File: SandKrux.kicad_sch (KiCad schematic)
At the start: 55 parts, among them CN1 527450697, J1 FH12-40S-0.5SH_55_, J2 Connector, USB-TYPE-C-16P, U1 K210_C913414, U2 AXP173, U3 MT9700-N, U5 GD25LQ128EWIGR, U6 TMI7003C, U7 SGM803-TXN3/TR_C5152602, X1 X322526MMB4SI

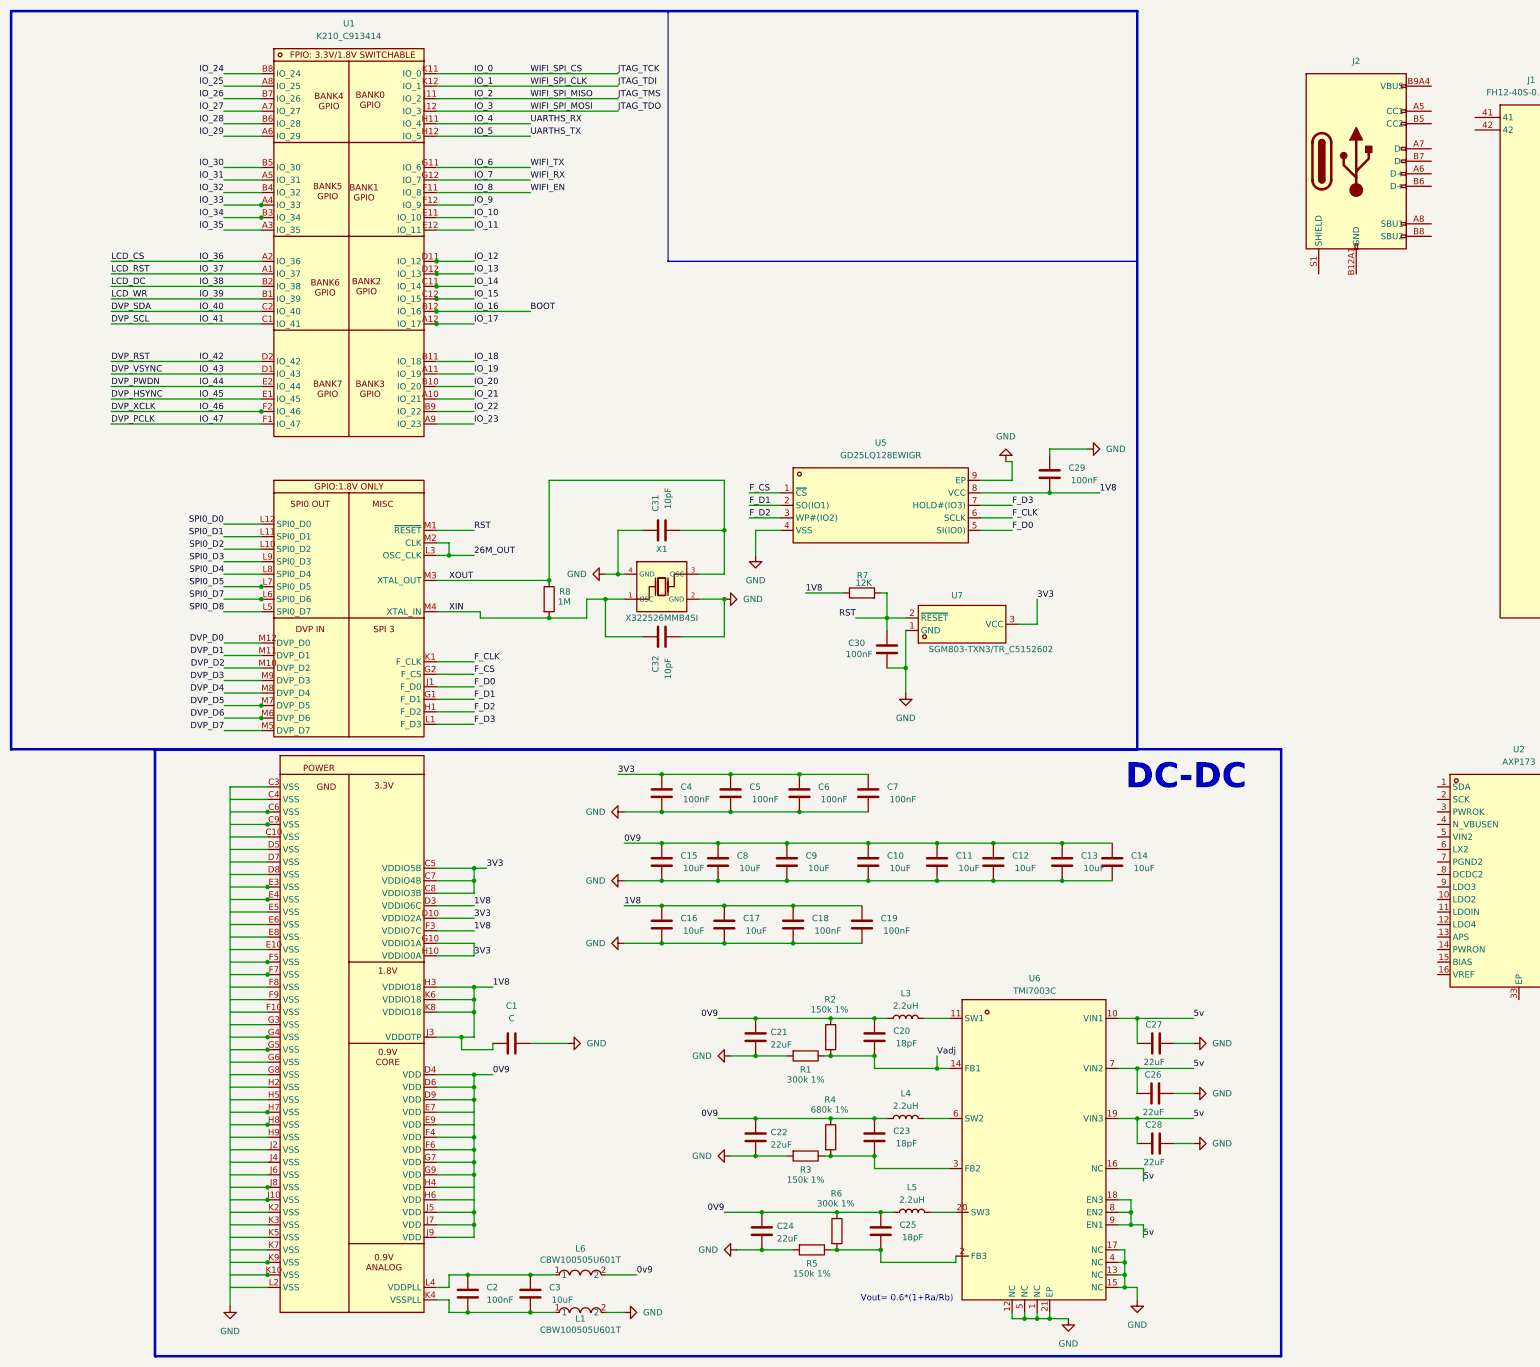
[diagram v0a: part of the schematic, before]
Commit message: camera suport
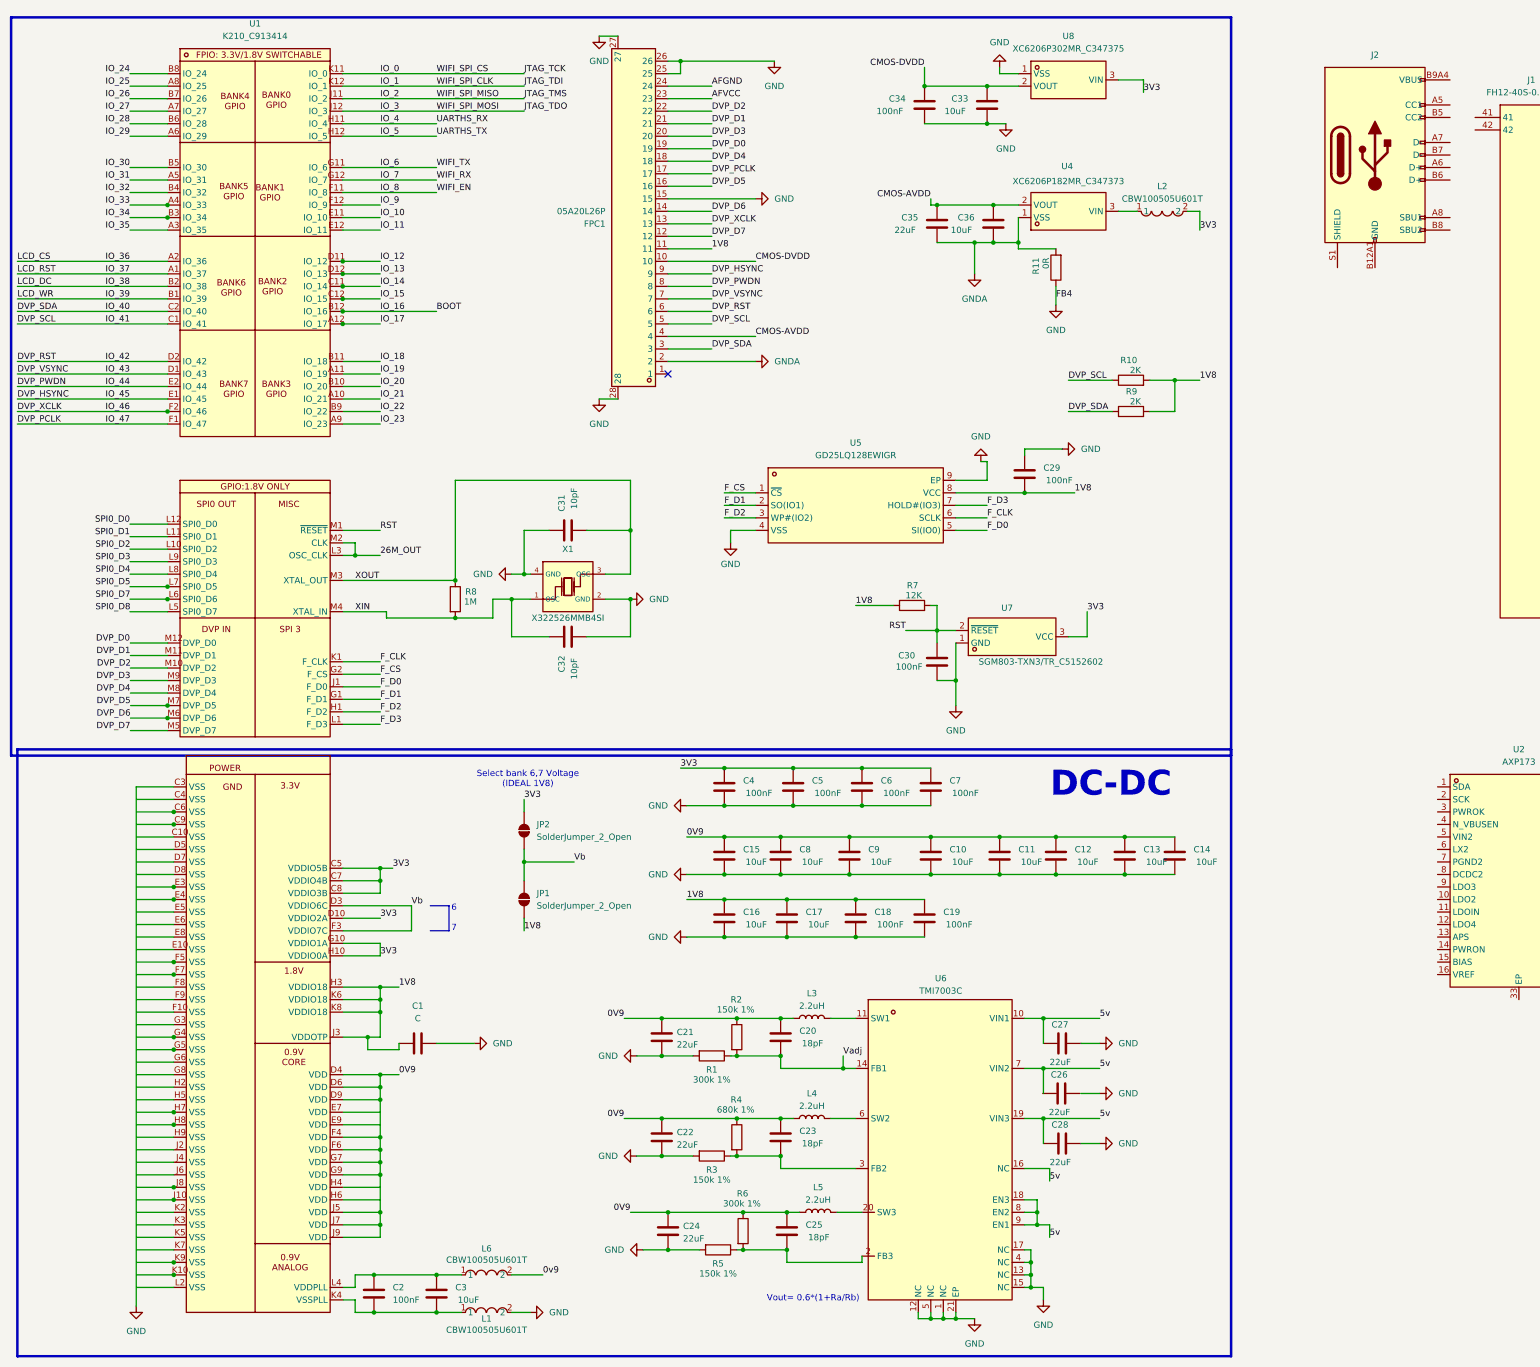
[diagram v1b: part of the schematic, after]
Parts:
- added C33, C36: 10uF, symbol Device:C
- added C34: 100nF, symbol Device:C
- added C35: 22uF, symbol Device:C
- added FPC1: 05A20L26P, easyeda2kicad:FPC-SMD_05A20L26P, symbol easyeda2kicad:05A20L26P
- added JP1, JP2: SolderJumper_2_Open, Jumper:SolderJumper-2_P1.3mm_Open_RoundedPad1.0x1.5mm, symbol Jumper:SolderJumper_2_Open
- added L2: CBW100505U601T, easyeda2kicad:L0402, symbol easyeda2kicad:CBW100505U601T
- added R10, R9: 2K, symbol Device:R
- added R11: 0R, symbol Device:R
- added U4: XC6206P182MR_C347373, easyeda2kicad:SOT-23-3_L3.0-W1.7-P0.95-LS2.9-BR, symbol easyeda2kicad:XC6206P182MR_C347373
- added U8: XC6206P302MR_C347375, easyeda2kicad:SOT-23-3_L3.0-W1.7-P0.95-LS2.9-BR, symbol easyeda2kicad:XC6206P302MR_C347375
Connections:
- net 1V8: now also FPC1.11, JP1.2 (B), R10.2, R9.2
- net DVP_D0: now also FPC1.19
- net DVP_D1: now also FPC1.21
- net DVP_D2: now also FPC1.22
- net DVP_D3: now also FPC1.20
- net DVP_D4: now also FPC1.18
- net DVP_D5: now also FPC1.16
- net DVP_D6: now also FPC1.14
- net DVP_D7: now also FPC1.12
- net DVP_HSYNC: now also FPC1.9
- net DVP_PCLK: now also FPC1.17
- net DVP_PWDN: now also FPC1.8
- net DVP_RST: now also FPC1.6
- net DVP_SCL: now also FPC1.5, R10.1
- net DVP_SDA: now also FPC1.3, R9.1
- net DVP_VSYNC: now also FPC1.7
- net DVP_XCLK: now also FPC1.13
- net GND: now also C33.1, C34.1, FPC1.15, FPC1.25, FPC1.26, FPC1.27, FPC1.28, R11.1, U8.1 (VSS)
- net at C4.2, C5.2, C6.2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: now also JP2.1 (A), L2.2, U8.3 (VIN)
- new net: L2.1, U4.3 (VIN)
- new net AFGND: FPC1.24
- new net AFVCC: FPC1.23
- new net CMOS-AVDD: C35.2, C36.2, FPC1.4, U4.2 (VOUT)
- new net CMOS-DVDD: C33.2, C34.2, FPC1.10, U8.2 (VOUT)
- new net GNDA: C35.1, C36.1, FPC1.2, R11.2, U4.1 (VSS)
- new net Vb: JP1.1 (A), JP2.2 (B)
- no-connect marks 0 -> 1
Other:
- note added: "6 7"
- note added: "Select bank 6,7 Voltage (IDEAL 1V8)"
- moved on the sheet: C1, C10, C11, C12, C13, C14, C15, C16, C17, C18, C19, C2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

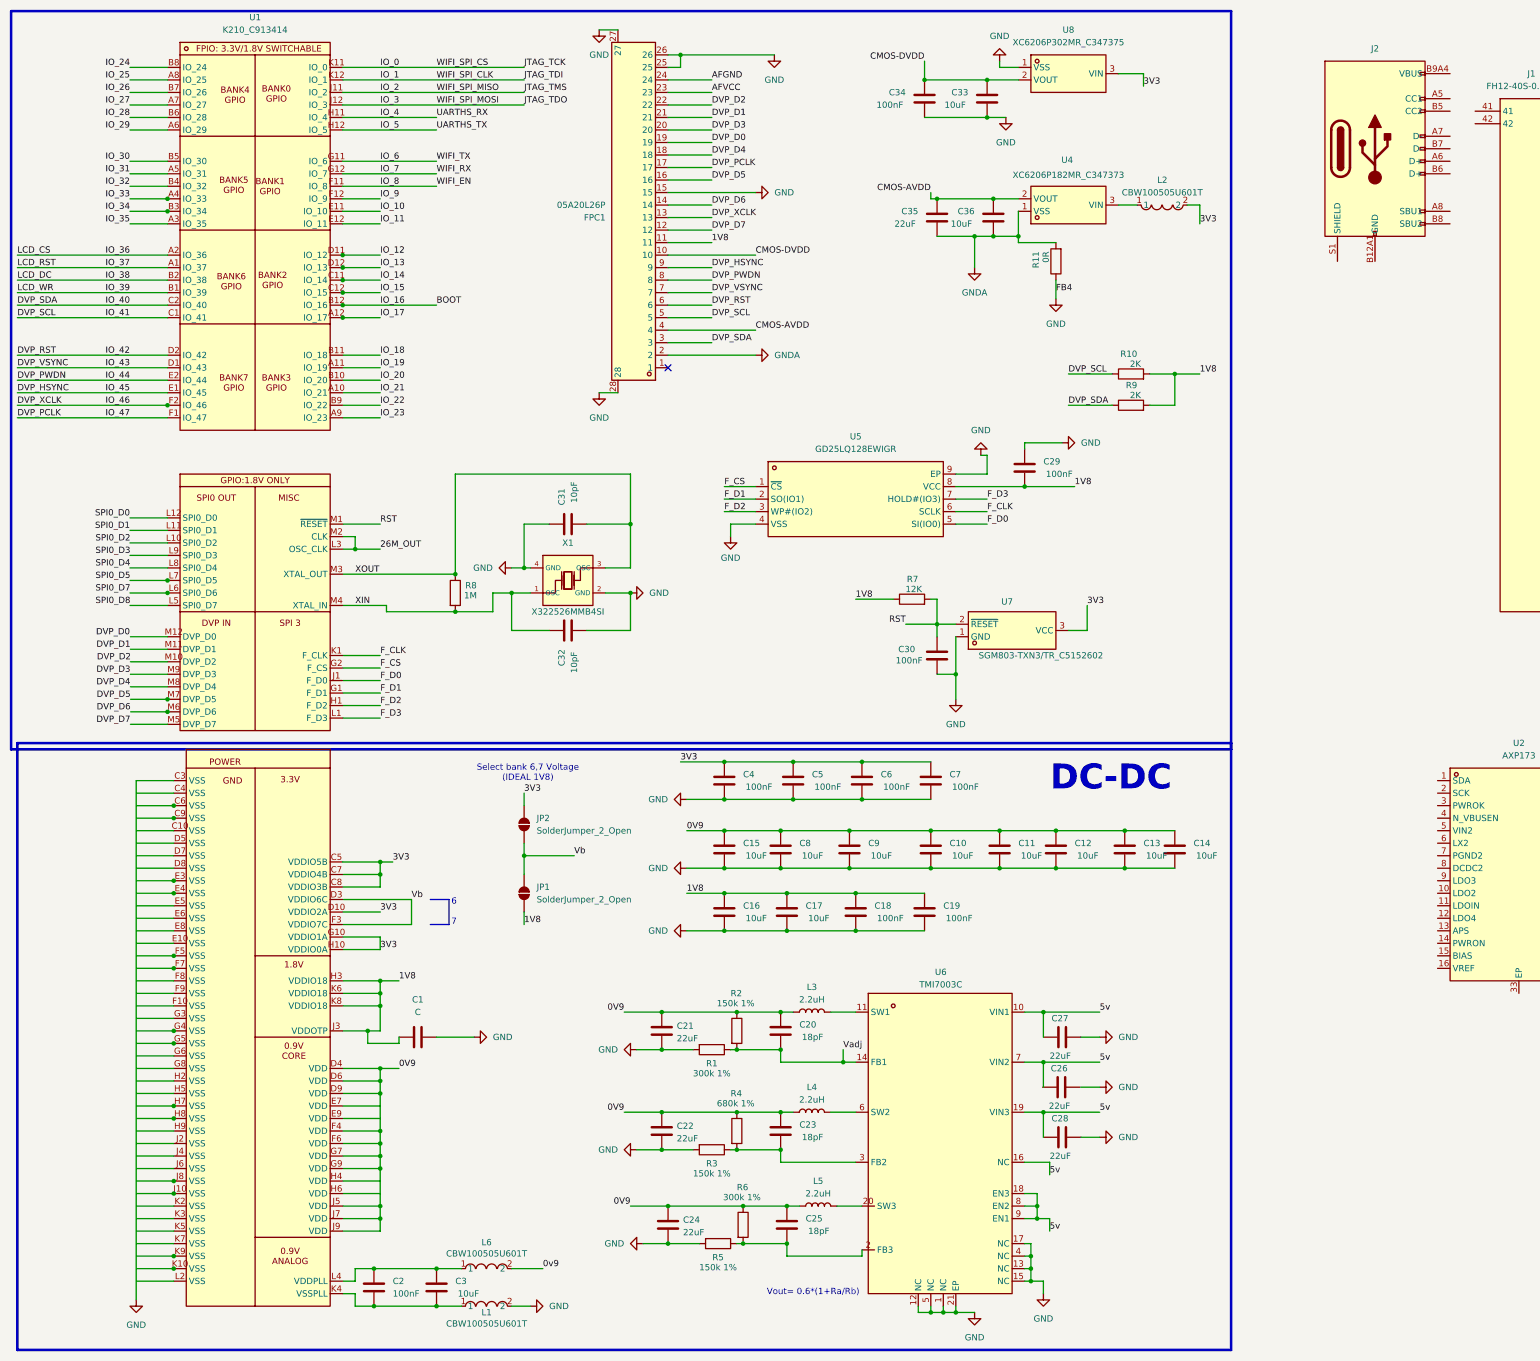
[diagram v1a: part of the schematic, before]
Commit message: organizacao basica dos componentes na pcb
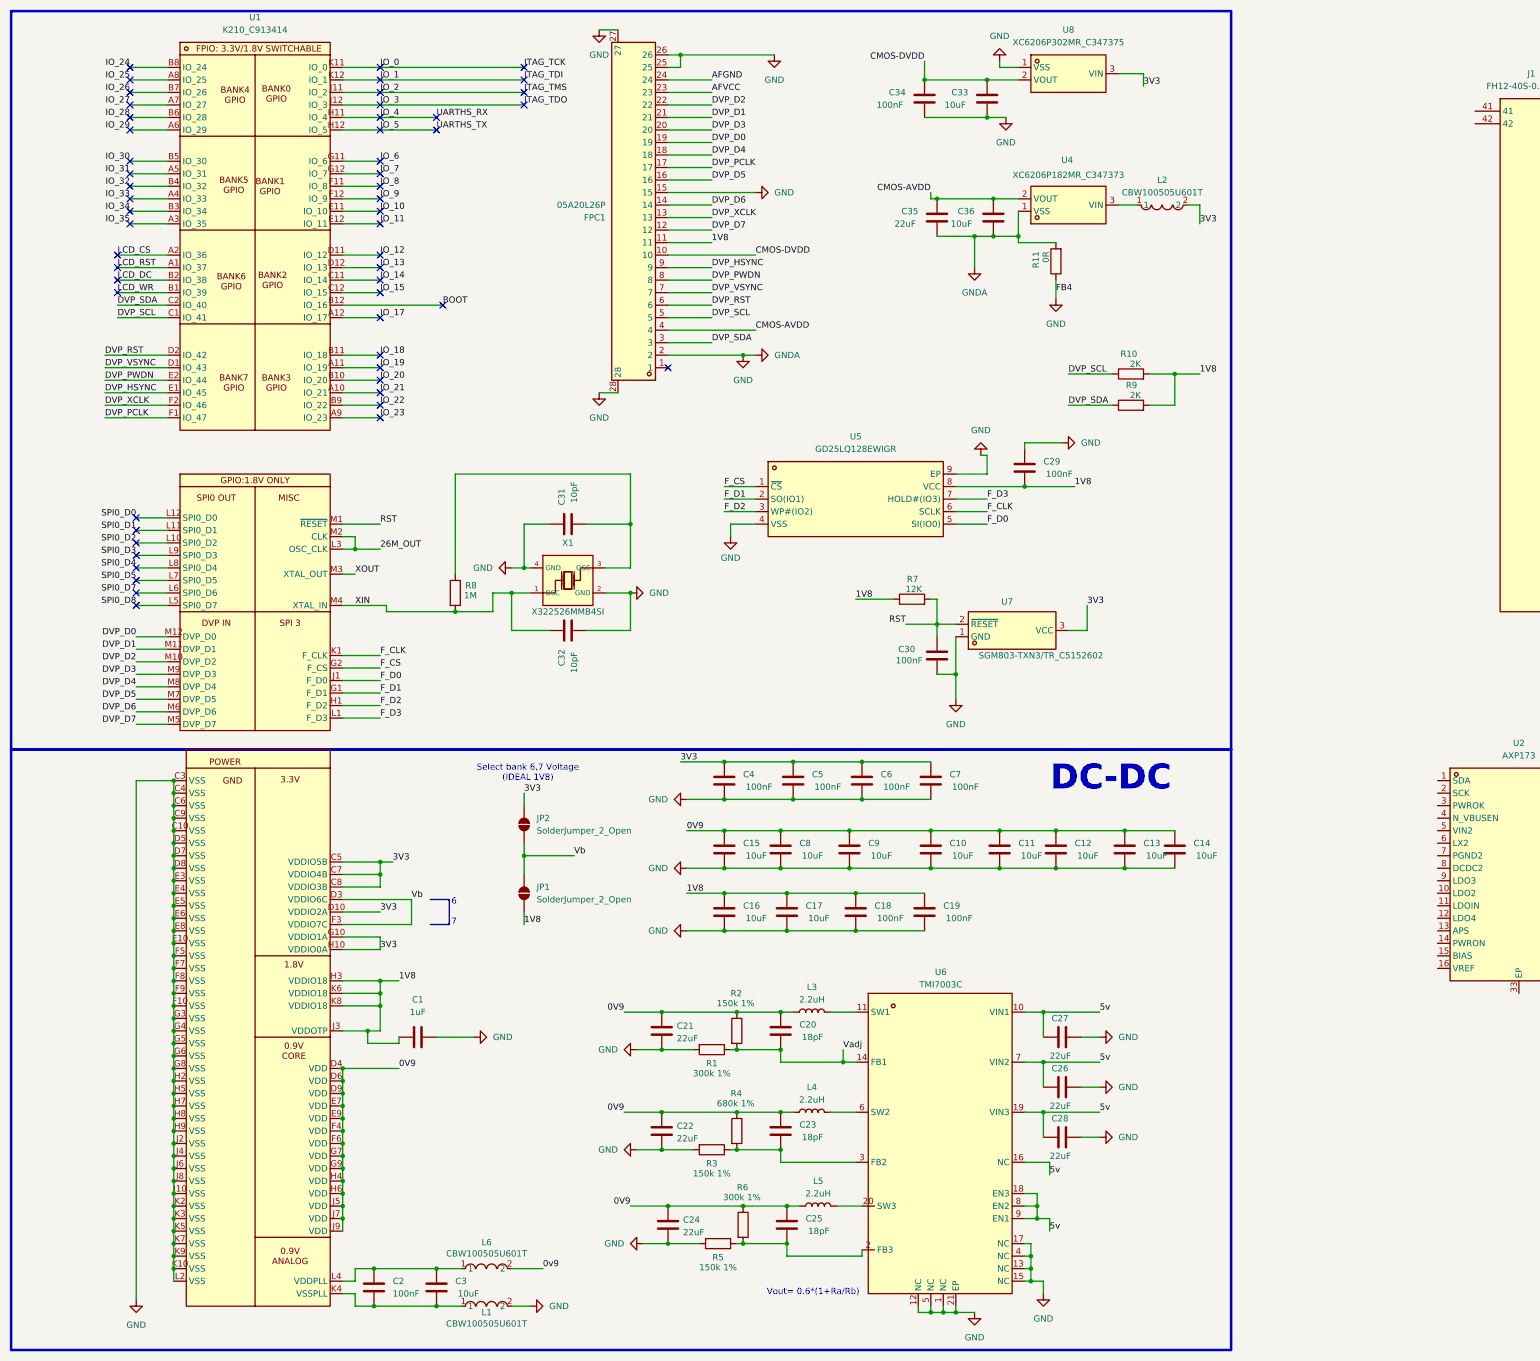
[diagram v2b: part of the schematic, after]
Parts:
- removed J2: Connector, USB-TYPE-C-16P, PCM_JLCPCB:TYPE-C-SMD_HX-TYPE-C-16PIN, symbol PCM_JLCPCB-Extended:Connector, USB-TYPE-C-16P
- C1: value C -> 1uF; footprint (none) -> Capacitor_SMD:C_0201_0603Metric
- C10, C11, C12, C13, C14, C15, C16, C17, C18, C19, C2, C20, C21, C22, C23, C24, C25, C26, C27, C28, C29, C3, C30, C31, C32, C33, C34, C35, C36, C4, C5, C6, C7, C8, C9: footprint (none) -> Capacitor_SMD:C_0201_0603Metric
- J1: footprint FH1240S05SH55 -> KiCad:FH1240S05SH55
- L3, L4, L5: footprint (none) -> Inductor_SMD:L_0805_2012Metric
- R1, R10, R11, R2, R3, R4, R5, R6, R7, R8, R9: footprint (none) -> Resistor_SMD:R_0201_0603Metric
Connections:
- net GNDA is gone; now on net GND: C35.1, C36.1, FPC1.2, R11.2, U4.1 (VSS)
- net 0V9: now also U1.D4 (VDD), U1.D6 (VDD), U1.D9 (VDD), U1.E7 (VDD), U1.E9 (VDD), U1.F4 (VDD), U1.F6 (VDD), U1.G7 (VDD), U1.G9 (VDD), U1.H4 (VDD), U1.H6 (VDD), U1.J5 (VDD), U1.J7 (VDD), U1.J9 (VDD)
- net 1V8: now also U1.H3 (VDDIO18), U1.J3 (VDDOTP), U1.K6 (VDDIO18), U1.K8 (VDDIO18)
- net 26M_OUT: now also U1.L3 (OSC_CLK), U1.M2 (CLK)
- net 5v: now also C26.2
- net DVP_D0: now also U1.M12 (DVP_D0)
- net F_CLK: now also U1.K1 (F_CLK)
- net F_CS: now also U1.G2 (F_CS)
- net F_D0: now also U1.J1 (F_D0)
- net F_D1: now also U1.G1 (F_D1)
- net F_D2: now also U1.H1 (F_D2)
- net F_D3: now also U1.L1 (F_D3)
- net GND: now also C26.1, U1.C10 (VSS), U1.C4 (VSS), U1.C6 (VSS), U1.C9 (VSS), U1.D5 (VSS), U1.D7 (VSS), U1.D8 (VSS), U1.E10 (VSS), U1.E3 (VSS), U1.E4 (VSS), U1.E5 (VSS), U1.E6 (VSS), U1.E8 (VSS), U1.F10 (VSS), U1.F5 (VSS), U1.F7 (VSS), U1.F8 (VSS), U1.F9 (VSS), U1.G3 (VSS), U1.G4 (VSS), U1.G5 (VSS), U1.G6 (VSS), U1.G8 (VSS), U1.H2 (VSS), U1.H5 (VSS), U1.H7 (VSS), U1.H8 (VSS), U1.H9 (VSS), U1.J10 (VSS), U1.J2 (VSS), U1.J4 (VSS), U1.J6 (VSS), U1.J8 (VSS), U1.K10 (VSS), U1.K2 (VSS), U1.K3 (VSS), U1.K5 (VSS), U1.K7 (VSS), U1.K9 (VSS), U1.L2 (VSS)
- net IO_18: now also U1.B11 (IO_18)
- net IO_19: now also U1.A11 (IO_19)
- net IO_20: now also U1.B10 (IO_20)
- net IO_21: now also U1.A10 (IO_21)
- net IO_22: now also U1.B9 (IO_22)
- net IO_23: now also U1.A9 (IO_23)
- net RST: now also U1.M1 (~{RESET})
- net Vb: now also U1.D3 (VDDIO6C), U1.F3 (VDDIO7C)
- net XIN: now also U1.M4 (XTAL_IN)
- net XOUT: now also U1.M3 (XTAL_OUT); no longer C31.1, R8.1, X1.3 (OSC)
- net at C4.2, C5.2, C6.2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: now also U1.C7 (VDDIO4B), U1.C8 (VDDIO3B), U1.D10 (VDDIO2A), U1.G10 (VDDIO1A), U1.H10 (VDDIO0A)
- net IO_36 renamed LCD_CS
- net IO_37 renamed LCD_RST
- net IO_38 renamed LCD_DC
- net IO_39 renamed LCD_WR
- new net: C31.1, R8.1, X1.3 (OSC)
- no-connect marks 1 -> 55
